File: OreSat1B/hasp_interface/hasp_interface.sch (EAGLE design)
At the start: 79 parts, among them J1 SAMTEC-MMS-104-02-X-SHJ, J2 ORESAT-DEBUG-CONNECTOR-ALL, Q1 MMBT2907SMD, U1 TCAN330, U10 TPS63070, U2 LM60440ARPKR, U7 STM32F091C, X1 16MHZ-2.5x2mm

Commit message: Wire cleanup
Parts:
- removed DB9: (no value), con-lstb:MA09-1
- removed EDAC: (no value), con-lstb:MA12-2
- added J3: MEC2-40-01-X-DV-WT, MEC2-40-01-X-DV-WT:MEC2-40-01-X-DV-WT
- added J5: TW-09-03-G-S-245-145, TW-09-03-G-S-245-145:TW-09-03-G-S-245-145
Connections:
- net +30VDC: now also J3.01, J3.02, J3.03, J3.04; no longer EDAC.1, EDAC.2, EDAC.3, EDAC.4
- net GND: now also J3.12, J3.18, J3.20, J3.21, J3.23; no longer EDAC.12, EDAC.18, EDAC.20, EDAC.21, EDAC.23
- net TURNSTILEFIRE-(DISCRETE1): now also J3.06; no longer EDAC.6

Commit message: Updated schematic
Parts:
- added R8: 10k, oresat-rcl:R-US_0603-C-NOSILK
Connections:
- removed net LT1618-ENABLE: U7.PA1
- removed net LT1618-IADJ: U7.PA4
- new net N$9: D2.A, R8.1
- net N$8: now also R8.2; no longer D2.A
- net TURNSTILEFIRE-(DISCRETE1): no longer J3.06

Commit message: Cleaned up and fixed errors on 30V SPS, removed some old solar module cruft.
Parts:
- removed D1: CMDD6001, D-Central-CMDD6001-silicon-low-leakage:CMDD6001
- removed Q1: MMBT2907SMD, Q-Diodesinc-MMBT2907-PNP:MMBT2907SMD
- removed R24, R25, R26, R27: 1k/NP, oresat-rcl:R-US_0603-C-NOSILK
- removed R8: 10k, oresat-rcl:R-US_0603-C-NOSILK
- removed U$1: FLIGHMARKERNEW, oresat-flight-marker:FLIGHMARKERNEW
- C1: value TBD -> 10u / 75V; DIS (none) -> Digi-Key; DPN (none) -> 490-12317-1-ND; MFR (none) -> Murata; MPN (none) -> GRT188R61C106KE13D
- R7: value TBD -> 1k
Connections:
- removed net N$4: C1.1, D1.A, Q1.B, R7.1
- removed net N$8: R8.2, U2.EN
- removed net SMSN0: R24.1, U7.PB12
- removed net SMSN1: R25.1, U7.PB13
- removed net SMSN2: R26.1, U7.PB14
- removed net SMSN3: R27.1, U7.PB15
- removed net TURNSTILEFIRE-(DISCRETE1): R3.2, U7.PB6
- net +30VDC: now also C1.1, R3.1
- net 3.3V: no longer R3.1
- net GND: now also J3.17, R7.2; no longer Q1.E, R24.2, R25.2, R26.2, R27.2
- net N$2: no longer Q1.C, R7.2
- net N$7: no longer D1.C, R4.2
- net N$9: now also R3.2, R7.1, U2.EN; no longer R8.1
- net VBUS: now also R4.2
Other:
- note added: "(29, 30, 33)V from HASP at 0.5 A (fused)"
- note added: "CHANGE TO DB9 M VERTICAL BOARD MOUNT"
- note added: "Vin = 36V max Iout = 4A"
- note added: "~ 3V (EN requires 1.2 V to turn on)"
- note removed: "Soft Start"
- note removed: "Solar module Serial Number Required by CAN messages. 0: +X+Z 1: -Y+Z 2: -X+Z 3: -Y+Z 4: +X-Z .. and so on."
- moved on the sheet: C1, C2, C3, C4, C5, C6, D7, J5, L2, R4, R5, R7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

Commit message: Added new cots dc dc converter and updated HASP interface connection.
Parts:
- removed C2: 100n, oresat-rcl:C-EU0603-C-NOSILK
- removed C3: TBD, oresat-rcl:C-EU0603-C-NOSILK
- removed C4: 10u, oresat-rcl:C-EU0603-C-NOSILK
- removed D2: 1N4448HLP-7, D-0402-package:D-0402
- removed J5: TW-09-03-G-S-245-145, TW-09-03-G-S-245-145:TW-09-03-G-S-245-145
- removed L2: L-BOURNS-SRN4018TA, L-Bourns-SRN4018TA:L-BOURNS-SRN4018TA
- removed R3: 10k, oresat-rcl:R-US_0603-C-NOSILK
- removed R4: TBD, oresat-rcl:R-US_0603-C-NOSILK
- removed R7: 1k, oresat-rcl:R-US_0603-C-NOSILK
- removed U2: LM60440ARPKR, U-TI-LM6044DRPKR-buck:LM60440ARPKR
- added U3: OKI-T/36W-W40, U-Murata-OKI-T36-W40-DC-DC-Converter:OKI-T/36W-W40
- C5: value 10u -> NP
- J3: value MEC2-40-01-X-DV-WT -> MOLEX-43045XXXX; device MEC2-40-01-X-DV-WT:MEC2-40-01-X-DV-WT -> J-Molex-043045XXXX-Dual-Row-Connector:MOLEX-43045XXXX
- R5: value TBD -> 3.8k
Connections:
- removed net N$5: C2.1, U2.BOOT
- removed net N$6: C3.1, U2.VCC
- removed net N$7: C2.2, L2.1, U2.SW
- removed net N$9: D2.A, R3.2, R7.1, U2.EN
- new net HASP_ANALOG_1: J3.4
- new net HASP_ANALOG_2: J3.3
- new net HASP_DISCRETE_1: J3.16
- new net HASP_DISCRETE_2: J3.15
- new net HASP_DISCRETE_3: J3.14
- new net HASP_DISCRETE_4: J3.13
- new net HASP_SERIAL_RX: J3.20
- new net HASP_SERIAL_TX: J3.10
- net !SHUTDOWN: no longer D2.C
- net +30VDC: now also J3.1, J3.11, J3.12, J3.2, U3.VIN; no longer J3.01, J3.02, J3.03, J3.04, R3.1, U2.VIN
- net GND: now also J3.5, J3.6, J3.7, J3.8, J3.9, U3.!EN, U3.GND; no longer C3.2, C4.2, J3.12, J3.20, J3.21, J3.23, R7.2, U2.AGND, U2.PGND
- net N$2: now also U3.TRIM; no longer R4.1, U2.FB
- net VBUS: now also U3.VOUT; no longer C4.1, L2.2, R4.2
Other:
- note added: "20 Pin connector to wires from DB9 and EDAC 516 connectors"
- note added: "29 V - 33 V from HASP at 0.5 A (fused)"
- note added: "OKI-T/36W-W40"
- note added: "Requires 2mm male shorting plug."
- note removed: "(29, 30, 33)V from HASP at 0.5 A (fused)"
- note removed: "CHANGE TO DB9 M VERTICAL BOARD MOUNT"
- note removed: "NOTE: DEBUG-1 powers solar module 3.3V directly from FT23X's onboard LDO on the DEBUG board. Schottky diode drops 3.3V LDO output to 3.0V; kicking in solar should be fine since 3.3 V > 3.0V which the diode will block."
- note removed: "ONLY POPULATED IN +Z+X SOLAR BOARD. DNP ALL OTHER BOARDS. Requires 2mm male shorting plug."
- note removed: "On EDAC: Pin 1 corresponds to pin A, Pin 2 corresponds to pin B, etc."
- note removed: "~ 3V (EN requires 1.2 V to turn on)"
- moved on the sheet: C1, C5, C6, R5

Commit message: Updated connector footprint and did layout
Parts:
- J3: value MOLEX-43045XXXX -> MOLEX-43045XXXXVERTICAL; device J-Molex-043045XXXX-Dual-Row-Connector:MOLEX-43045XXXX -> J-Molex-043045XXXX-Dual-Row-Connector:MOLEX-43045XXXXVERTICAL
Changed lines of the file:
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@@
 <setting verticaltext="up"/>
 </settings>
-<grid distance="0.025" unitdist="inch" unit="inch" style="lines" multiple="1" display="no" altdistance="0.01" altunitdist="inch" altunit="inch"/>
+<grid distance="0.01" unitdist="inch" unit="inch" style="lines" multiple="1" display="yes" altdistance="0.01" altunitdist="inch" altunit="inch"/>
 <layers>
 <layer number="1" name="Top" color="4" fill="1" visible="no" active="no"/>
@@
 <part name="GND5" library="supply1" library_urn="urn:adsk.eagle:library:371" deviceset="GND" device=""/>
 <part name="U3" library="U-Murata-OKI-T36-W40-DC-DC-Converter" deviceset="OKI-T/36W-W40" device=""/>
-<part name="J3" library="J-Molex-043045XXXX-Dual-Row-Connector" deviceset="MOLEX-43045XXXX" device=""/>
+<part name="J3" library="J-Molex-043045XXXX-Dual-Row-Connector" deviceset="MOLEX-43045XXXX" device="VERTICAL"/>
 <part name="GND2" library="supply1" library_urn="urn:adsk.eagle:library:371" deviceset="GND" device=""/>
 <part name="GND3" library="supply1" library_urn="urn:adsk.eagle:library:371" deviceset="GND" device=""/>

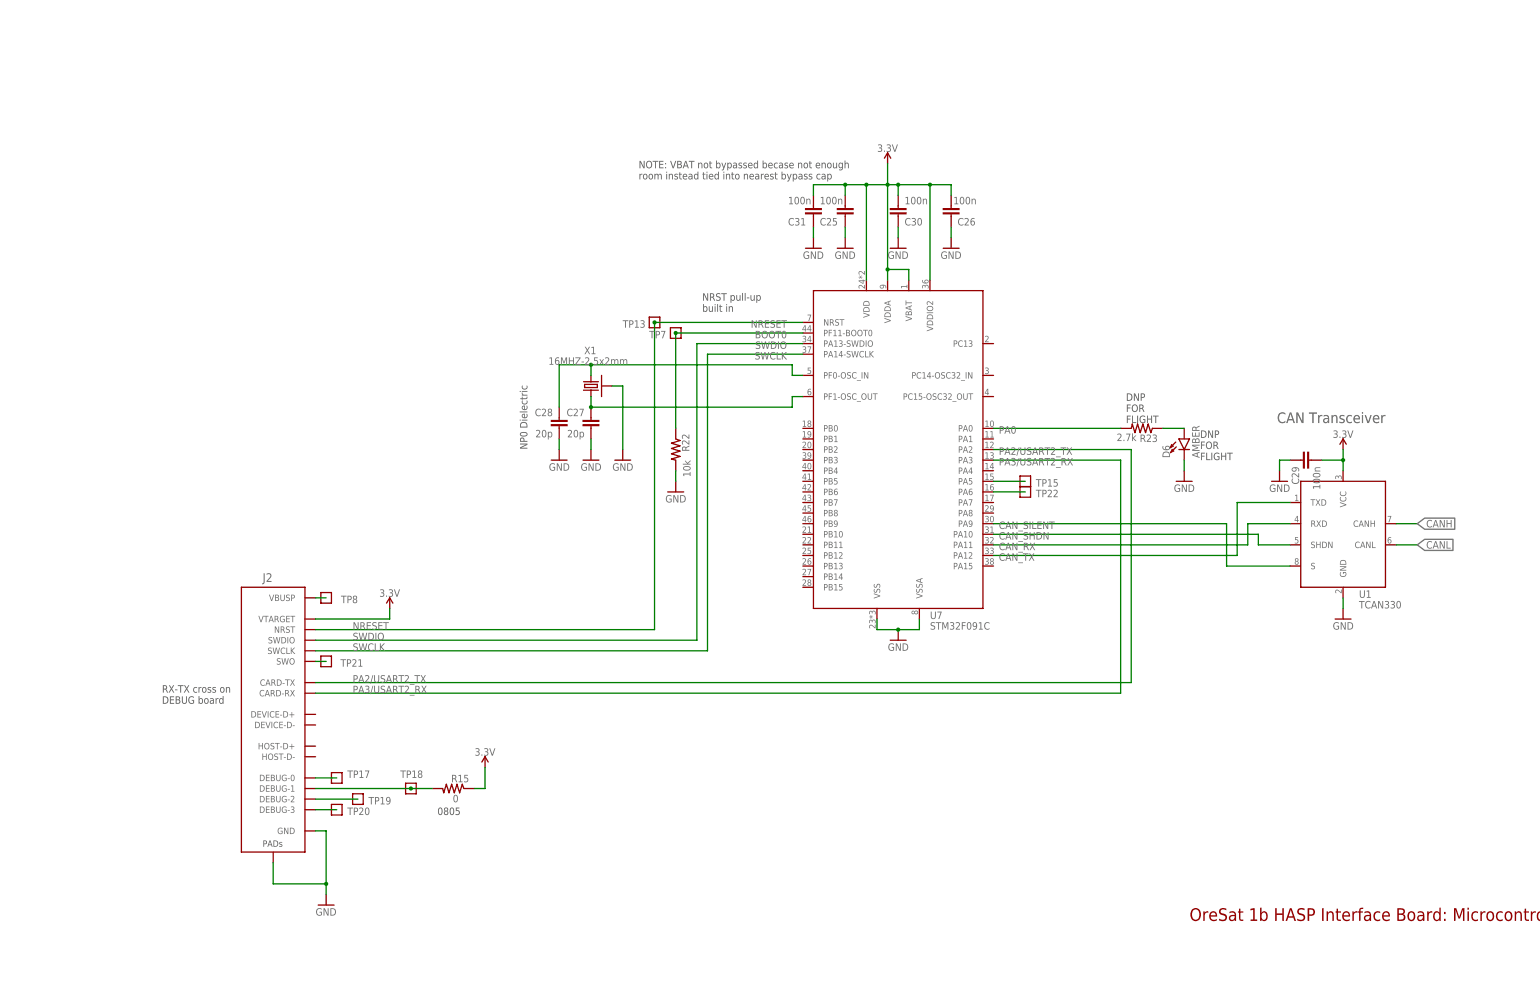
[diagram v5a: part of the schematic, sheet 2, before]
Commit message: Added RS232 level converter in case we want it. Added DAC outputs to HASP analog inputs in case we want it. Moved main connector out of fastener's way. Cleanup.
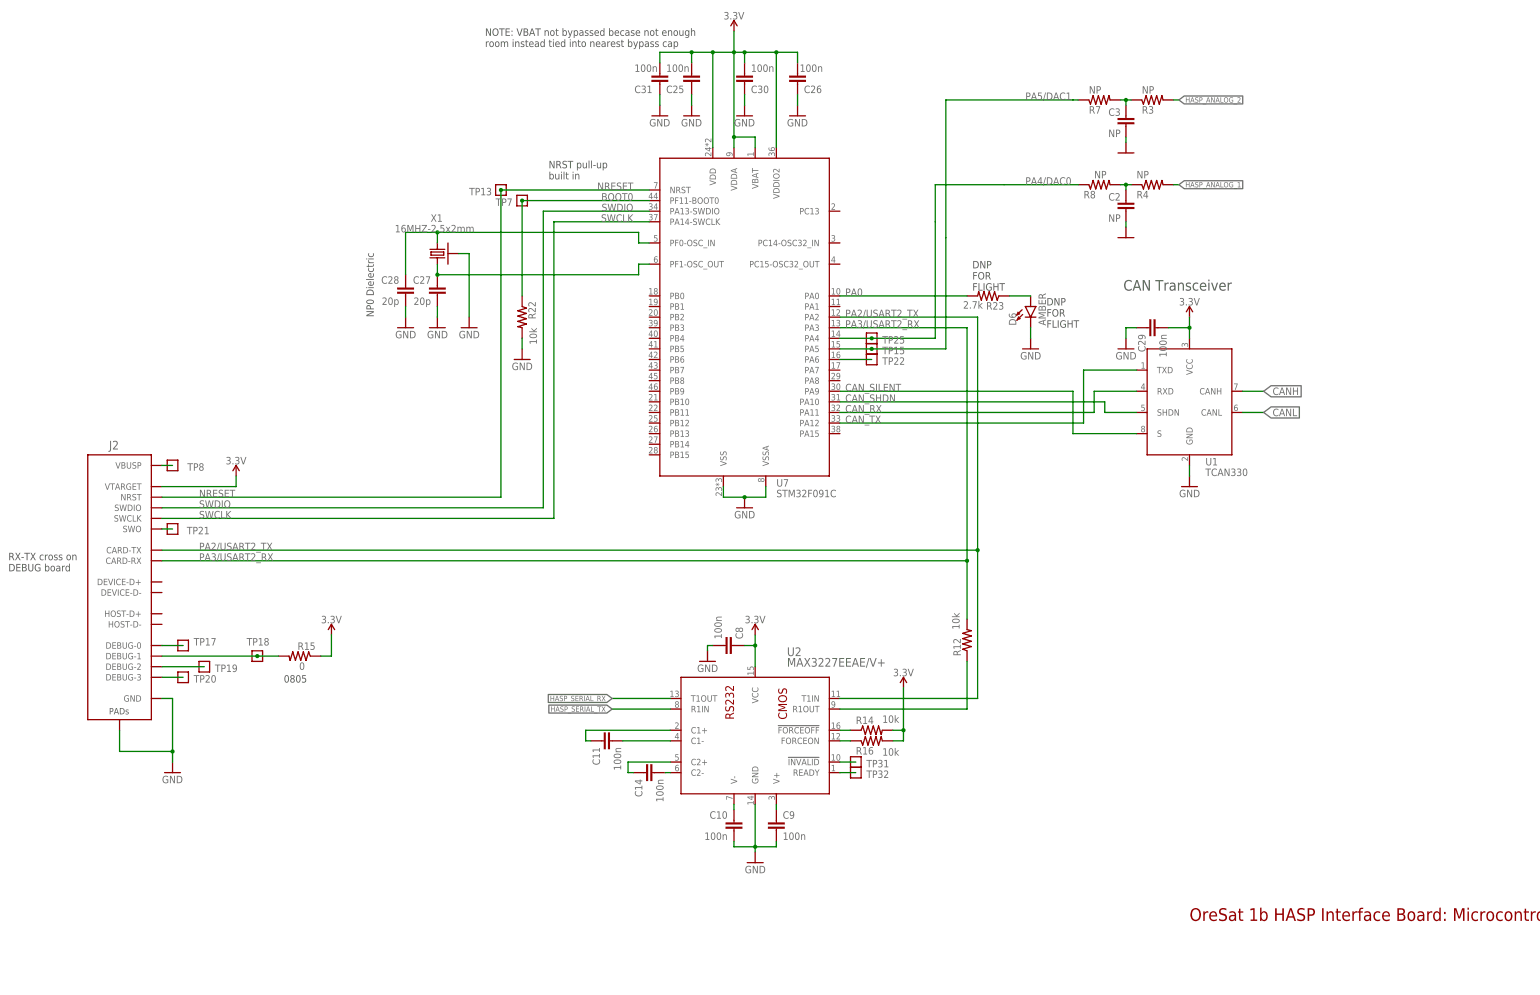
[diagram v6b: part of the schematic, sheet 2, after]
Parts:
- added C10, C11, C14, C8, C9: 100n, oresat-rcl:C-EU0603-C-NOSILK
- added C2, C3: NP, oresat-rcl:C-EU0603-C-NOSILK
- added C4: 10u 60V, oresat-rcl:C-EU1206-C
- added R10: 3.8k, oresat-rcl:R-US_0603-C-NOSILK
- added R12, R14, R16: 10k, oresat-rcl:R-US_0603-C-NOSILK
- added R3, R4, R7, R8: NP, oresat-rcl:R-US_0603-C-NOSILK
- added TP10, TP12, TP14, TP16, TP2, TP23, TP24, TP25, TP3, TP30, TP31, TP32, TP4, TP5: TEST-POINT-LARGE-SQUARE, oresat-misc:TEST-POINT-LARGE-SQUARE
- added U2: MAX3227EEAE/V+, U-Maxim-MAX3227-RS232-transceiver-driver:MAX3227EEAE/V+
- C1: value 10u / 75V -> 10U 60V; device oresat-rcl:C-EU0603-C-NOSILK -> oresat-rcl:C-EU1206-C; DIS Digi-Key -> (none); DPN 490-12317-1-ND -> (none); MFR Murata -> (none); MPN GRT188R61C106KE13D -> (none)
- J3: value MOLEX-43045XXXXVERTICAL -> MOLEX-43045XXXXRIGHTANGLE; device J-Molex-043045XXXX-Dual-Row-Connector:MOLEX-43045XXXXVERTICAL -> J-Molex-043045XXXX-Dual-Row-Connector:MOLEX-43045XXXXRIGHTANGLE
- U3: value OKI-T/36W-W40 -> OKI-T/36W-W40N
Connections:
- removed net PA5: TP15.1, U7.PA5
- new net N$10: C14.1, U2.C2+
- new net N$11: C11.2, U2.C1-
- new net N$12: C11.1, U2.C1+
- new net N$13: R12.1, U2.R1OUT
- new net N$15: R16.1, U2.FORCEON
- new net N$17: TP31.1, U2.!INVALID
- new net N$18: TP32.1, U2.READY
- new net N$3: C3.1, R3.1, R7.2
- new net N$4: C2.1, R4.1, R8.2
- new net N$5: R10.2, TP30.1, U3.!EN
- new net N$6: R14.1, U2.!FORCEOFF
- new net N$7: C10.1, U2.V-
- new net N$8: C9.1, U2.V+
- new net N$9: C14.2, U2.C2-
- new net PA4/DAC0: R8.1, TP25.1, U7.PA4
- new net PA5/DAC1: R7.1, TP15.1, U7.PA5
- net +30VDC: now also C4.1, TP2.1
- net 3.3V: now also C8.1, R14.2, R16.2, U2.VCC
- net GND: now also C10.2, C2.2, C3.2, C4.2, C8.2, C9.2, J3.13, J3.14, J3.19, J3.3, J3.4, R10.1, U2.GND; no longer J3.17, J3.18, J3.5, J3.6, U3.!EN
- net HASP_ANALOG_1: now also J3.6, R4.2, TP5.1; no longer J3.4
- net HASP_ANALOG_2: now also J3.5, R3.2, TP4.1; no longer J3.3
- net HASP_DISCRETE_1: now also J3.18, TP14.1; no longer J3.16
- net HASP_DISCRETE_2: now also J3.17, TP16.1; no longer J3.15
- net HASP_DISCRETE_3: now also J3.16, TP23.1; no longer J3.14
- net HASP_DISCRETE_4: now also J3.15, TP24.1; no longer J3.13
- net HASP_SERIAL_RX: now also TP12.1, U2.T1OUT
- net HASP_SERIAL_TX: now also TP10.1, U2.R1IN
- net PA2/USART2_TX: now also U2.T1IN
- net PA3/USART2_RX: now also R12.2
- net VBUS: now also TP3.1
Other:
- note added: "1206"
- note added: "29 V - 33 V from HASP at 0.5 A (fused, w/1.5A inrush)"
- note added: "All "DISCRETE" lines are NC for HASP Small Paylods"
- note added: "OKI-T/36W-W40N"
- note removed: "29 V - 33 V from HASP at 0.5 A (fused)"
- note removed: "OKI-T/36W-W40"
- moved on the sheet: C1, C25, C26, C27, C28, C29, C30, C31, D6, J2, J3, R15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
